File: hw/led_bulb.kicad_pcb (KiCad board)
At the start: 2 copper layers, 136 x 50 mm, 181 parts, among them P1 USB_OTG, P10 CONN_01X04, P11 CONN_01X04, P12 CONN_01X04, P13 CONN_01X04, P14 CONN_01X04, P15 CONN_01X04, P16 CONN_01X04, P17 CONN_01X04, P2 CONN_01X04, P3 CONN_01X04, P4 CONN_01X04, P5 CONN_01X04, P6 CONN_01X04, P7 CONN_01X04, P8 CONN_01X04, P9 CONN_01X04, SW1 SW_RST, SW2 SW_FLASH, U1 CP2102, U3 ESP-12E, U4 AP1117D33

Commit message: Added first version of v4 hardware.
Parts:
- removed HOLE0 (x88): 0.3mm, footprints:0.3mm
- added P18: CONN_01X02, footprints:CONN_2.54mm_1x2_no-outline, F.Cu at (156.4, 125.6)
- added P19: CONN_01X02, footprints:CONN_2.54mm_1x2_no-outline, F.Cu at (149.2, 125.5)
- added P20: CONN_01X02, footprints:CONN_2.54mm_1x2_no-outline, F.Cu at (172.8, 149.2)
- added P21: CONN_01X02, footprints:CONN_2.54mm_1x2_no-outline, F.Cu at (172.8, 142.0)
- added P22: CONN_01X02, footprints:CONN_2.54mm_1x2_no-outline, F.Cu at (149.2, 165.6)
- added P23: CONN_01X02, footprints:CONN_2.54mm_1x2_no-outline, F.Cu at (156.4, 165.6)
- added P24: CONN_01X02, footprints:CONN_2.54mm_1x2_no-outline, F.Cu at (132.9, 142.1)
- added P25: CONN_01X02, footprints:CONN_2.54mm_1x2_no-outline, F.Cu at (132.9, 149.2)
- added P26: CONN_01X02, footprints:CONN_2.54mm_1x2_no-outline, F.Cu at (109.0, 85.1)
- added P27: CONN_01X02, footprints:CONN_2.54mm_1x2_no-outline, F.Cu at (109.0, 78.0)
- added P28: CONN_01X02, footprints:CONN_2.54mm_1x2_no-outline, F.Cu at (109.0, 96.8)
- added P29: CONN_01X02, footprints:CONN_2.54mm_1x2_no-outline, F.Cu at (109.0, 89.7)
- added P30: CONN_01X02, footprints:CONN_2.54mm_1x2_no-outline, F.Cu at (109.0, 108.3)
- added P31: CONN_01X02, footprints:CONN_2.54mm_1x2_no-outline, F.Cu at (109.0, 101.1)
- added P32: CONN_01X02, footprints:CONN_2.54mm_1x2_no-outline, F.Cu at (109.0, 119.7)
- added P33: CONN_01X02, footprints:CONN_2.54mm_1x2_no-outline, F.Cu at (109.0, 112.5)
- P10, P11, P12, P13, P14, P15, P16, P17, P2, P3, P4, P5, P6, P7, P8, P9: value CONN_01X04 -> CONN_01X02; footprint footprints:CONN_2.54mm_1x4_no-outline -> footprints:CONN_2.54mm_1x2_no-outline
- SW1, SW2: footprint footprints:switch_spst_smd_5.5mm_4.5mm -> footprints:switch_spst_smd_5mm_3.5mm
- moved P5 150.2 mm to (102.1, 165.3), turned to 90 degrees
- moved R9 124.8 mm to (112.5, 152.7)
- moved P2 124.1 mm to (102.1, 125.5), turned to 270 degrees
- moved LED9 122.9 mm to (105.7, 126.2)
- moved LED3 122.8 mm to (105.7, 152.2)
- moved LED5 122.8 mm to (105.7, 132.6)
- moved LED11 122.7 mm to (105.8, 165.1)
- moved LED7 122.7 mm to (105.8, 158.6)
- moved LED1 122.6 mm to (105.7, 139.1)
- moved P1 122.6 mm to (103.8, 149.0)
- moved LED12 122.6 mm to (86.2, 145.6)
- moved LED6 122.6 mm to (118.7, 145.6)
- moved C5 122.6 mm to (109.8, 158.0)
- moved C6 122.6 mm to (109.8, 156.3)
- moved LED2 122.6 mm to (112.1, 145.6)
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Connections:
- net DTR renamed Net-(U1-Pad28)
- net RTS renamed Net-(U1-Pad24)
- LED1 pad 1: GPIO16 -> GPIO0
- LED13 pad 3: GND -> Net-(LED13-Pad3)
- LED13 pad 4: V_USB -> Net-(LED13-Pad4)
- LED14 pad 3: GND -> Net-(LED14-Pad3)
- LED14 pad 4: V_USB -> Net-(LED14-Pad4)
- LED15 pad 3: GND -> Net-(LED15-Pad3)
- LED15 pad 4: V_USB -> Net-(LED15-Pad4)
- LED16 pad 3: GND -> Net-(LED16-Pad3)
- LED16 pad 4: V_USB -> Net-(LED16-Pad4)
- LED17 pad 3: GND -> Net-(LED13-Pad3)
- LED17 pad 4: V_USB -> Net-(LED13-Pad4)
- LED18 pad 3: GND -> Net-(LED14-Pad3)
- LED18 pad 4: V_USB -> Net-(LED14-Pad4)
- LED19 pad 3: GND -> Net-(LED15-Pad3)
- LED19 pad 4: V_USB -> Net-(LED15-Pad4)
- LED20 pad 3: GND -> Net-(LED16-Pad3)
- LED20 pad 4: V_USB -> Net-(LED16-Pad4)
- LED21 pad 3: GND -> Net-(LED13-Pad3)
- LED21 pad 4: V_USB -> Net-(LED13-Pad4)
- LED22 pad 3: GND -> Net-(LED14-Pad3)
- LED22 pad 4: V_USB -> Net-(LED14-Pad4)
- LED23 pad 3: GND -> Net-(LED15-Pad3)
- LED23 pad 4: V_USB -> Net-(LED15-Pad4)
- LED24 pad 3: GND -> Net-(LED16-Pad3)
- LED24 pad 4: V_USB -> Net-(LED16-Pad4)
- LED25 pad 3: GND -> Net-(LED13-Pad3)
- LED25 pad 4: V_USB -> Net-(LED13-Pad4)
- LED26 pad 3: GND -> Net-(LED14-Pad3)
- LED26 pad 4: V_USB -> Net-(LED14-Pad4)
- LED27 pad 3: GND -> Net-(LED15-Pad3)
- LED27 pad 4: V_USB -> Net-(LED15-Pad4)
- LED28 pad 3: GND -> Net-(LED16-Pad3)
- LED28 pad 4: V_USB -> Net-(LED16-Pad4)
- LED29 pad 3: GND -> Net-(LED13-Pad3)
- LED29 pad 4: V_USB -> Net-(LED13-Pad4)
- LED30 pad 3: GND -> Net-(LED14-Pad3)
- LED30 pad 4: V_USB -> Net-(LED14-Pad4)
- LED31 pad 3: GND -> Net-(LED15-Pad3)
- LED31 pad 4: V_USB -> Net-(LED15-Pad4)
- LED32 pad 3: GND -> Net-(LED16-Pad3)
- LED32 pad 4: V_USB -> Net-(LED16-Pad4)
- LED33 pad 3: GND -> Net-(LED13-Pad3)
- LED33 pad 4: V_USB -> Net-(LED13-Pad4)
- LED34 pad 3: GND -> Net-(LED14-Pad3)
- LED34 pad 4: V_USB -> Net-(LED14-Pad4)
- LED35 pad 3: GND -> Net-(LED15-Pad3)
- LED35 pad 4: V_USB -> Net-(LED15-Pad4)
- LED36 pad 3: GND -> Net-(LED16-Pad3)
- LED36 pad 4: V_USB -> Net-(LED16-Pad4)
- LED37 pad 3: GND -> Net-(LED13-Pad3)
- LED37 pad 4: V_USB -> Net-(LED13-Pad4)
- LED38 pad 3: GND -> Net-(LED14-Pad3)
- LED38 pad 4: V_USB -> Net-(LED14-Pad4)
- LED39 pad 3: GND -> Net-(LED15-Pad3)
- LED39 pad 4: V_USB -> Net-(LED15-Pad4)
- LED40 pad 3: GND -> Net-(LED16-Pad3)
- LED40 pad 4: V_USB -> Net-(LED16-Pad4)
- LED41 pad 3: GND -> Net-(LED41-Pad3)
- LED41 pad 4: V_USB -> Net-(LED41-Pad4)
- LED42 pad 3: GND -> Net-(LED42-Pad3)
- LED42 pad 4: V_USB -> Net-(LED42-Pad4)
- LED43 pad 3: GND -> Net-(LED43-Pad3)
- LED43 pad 4: V_USB -> Net-(LED43-Pad4)
- LED44 pad 3: GND -> Net-(LED44-Pad3)
- LED44 pad 4: V_USB -> Net-(LED44-Pad4)
- LED45 pad 3: GND -> Net-(LED42-Pad3)
- LED45 pad 4: V_USB -> Net-(LED42-Pad4)
- LED46 pad 3: GND -> Net-(LED41-Pad3)
- LED46 pad 4: V_USB -> Net-(LED41-Pad4)
- LED47 pad 3: GND -> Net-(LED43-Pad3)
- LED47 pad 4: V_USB -> Net-(LED43-Pad4)
- LED48 pad 3: GND -> Net-(LED44-Pad3)
- LED48 pad 4: V_USB -> Net-(LED44-Pad4)
- LED49 pad 3: GND -> Net-(LED42-Pad3)
- LED49 pad 4: V_USB -> Net-(LED42-Pad4)
- LED50 pad 3: GND -> Net-(LED41-Pad3)
- LED50 pad 4: V_USB -> Net-(LED41-Pad4)
- LED51 pad 3: GND -> Net-(LED43-Pad3)
- LED51 pad 4: V_USB -> Net-(LED43-Pad4)
- LED52 pad 3: GND -> Net-(LED44-Pad3)
- LED52 pad 4: V_USB -> Net-(LED44-Pad4)
- LED53 pad 3: GND -> Net-(LED41-Pad3)
- LED53 pad 4: V_USB -> Net-(LED41-Pad4)
- P10 pad 1: Net-(LED37-Pad6) -> Net-(LED13-Pad2)
- P10 pad 2: Net-(LED37-Pad5) -> Net-(LED13-Pad1)
- P11 pad 1: Net-(LED38-Pad6) -> Net-(LED13-Pad3)
- P11 pad 2: Net-(LED38-Pad5) -> Net-(LED13-Pad4)
- P12 pad 1: Net-(LED39-Pad6) -> Net-(LED14-Pad2)
- P12 pad 2: Net-(LED39-Pad5) -> Net-(LED14-Pad1)
- P13 pad 1: Net-(LED40-Pad6) -> Net-(LED14-Pad3)
- P13 pad 2: Net-(LED40-Pad5) -> Net-(LED14-Pad4)
- P14 pad 1: GND -> Net-(LED15-Pad2)
- P14 pad 2: V_USB -> Net-(LED15-Pad1)
- P15 pad 1: GND -> Net-(LED15-Pad3)
- P15 pad 2: V_USB -> Net-(LED15-Pad4)
- P16 pad 1: GND -> Net-(LED16-Pad2)
- P16 pad 2: V_USB -> Net-(LED16-Pad1)
- P17 pad 1: GND -> Net-(LED16-Pad3)
- P17 pad 2: V_USB -> Net-(LED16-Pad4)
- P3 pad 1: Net-(LED10-Pad6) -> V_USB
- P3 pad 2: Net-(LED10-Pad5) -> GND
- P4 pad 1: Net-(LED11-Pad6) -> Net-(LED10-Pad6)
- P4 pad 2: Net-(LED11-Pad5) -> Net-(LED10-Pad5)
- P5 pad 1: Net-(LED12-Pad6) -> V_USB
- P5 pad 2: Net-(LED12-Pad5) -> GND
- P6 pad 1: GND -> Net-(LED11-Pad6)
- P6 pad 2: V_USB -> Net-(LED11-Pad5)
- P7 pad 1: GND -> V_USB
- P7 pad 2: V_USB -> GND
- P8 pad 1: GND -> Net-(LED12-Pad6)
- P8 pad 2: V_USB -> Net-(LED12-Pad5)
- P9 pad 1: GND -> V_USB
- P9 pad 2: V_USB -> GND
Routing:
- net GND: track 595.8 -> 0.00 mm, vias 30 -> 0
- net V_USB: track 508.1 -> 0.00 mm, vias 42 -> 0
- net V_3.3: track 76.2 -> 0.00 mm, vias 3 -> 0
- net GPIO16: track 28.6 -> 0.00 mm, vias 1 -> 0
- net TX: track 27.7 -> 0.00 mm, vias 3 -> 0
- net Net-(R8-Pad1): track 21.2 -> 0.00 mm, vias 1 -> 0
- net GPIO0: track 18.6 -> 0.00 mm
- net GPIO2: track 16.8 -> 0.00 mm, vias 1 -> 0
- net nRST: track 12.5 -> 0.00 mm
- net GPIO15: track 12.2 -> 0.00 mm, vias 1 -> 0
- net USB_D+: track 11.5 -> 0.00 mm, vias 2 -> 0
- net USB_D-: track 9.94 -> 0.00 mm, vias 1 -> 0
- net EN: track 9.22 -> 0.00 mm
- net LED4_DATA: track 8.03 -> 0.00 mm, vias 1 -> 0
- net LED2_CLK: track 7.80 -> 0.00 mm, vias 1 -> 0
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- removed copper zone on B.Cu, net GND
- removed copper zone on B.Cu, net V_USB
- removed copper zone on F.Cu, net V_USB
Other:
- board size 136 x 50 mm -> 92.4 x 91.4 mm
- board text added: "esp8266_apa102_bulb v4"
- board text removed: "CLK_IN"
- board text removed: "CLK_OUT"
- board text removed: "D_IN"
- board text removed: "D_OUT"
- board text removed: "GND"
- board text removed: "VCC"
- board text removed: "esp8266_apa102_bulb v3.0"

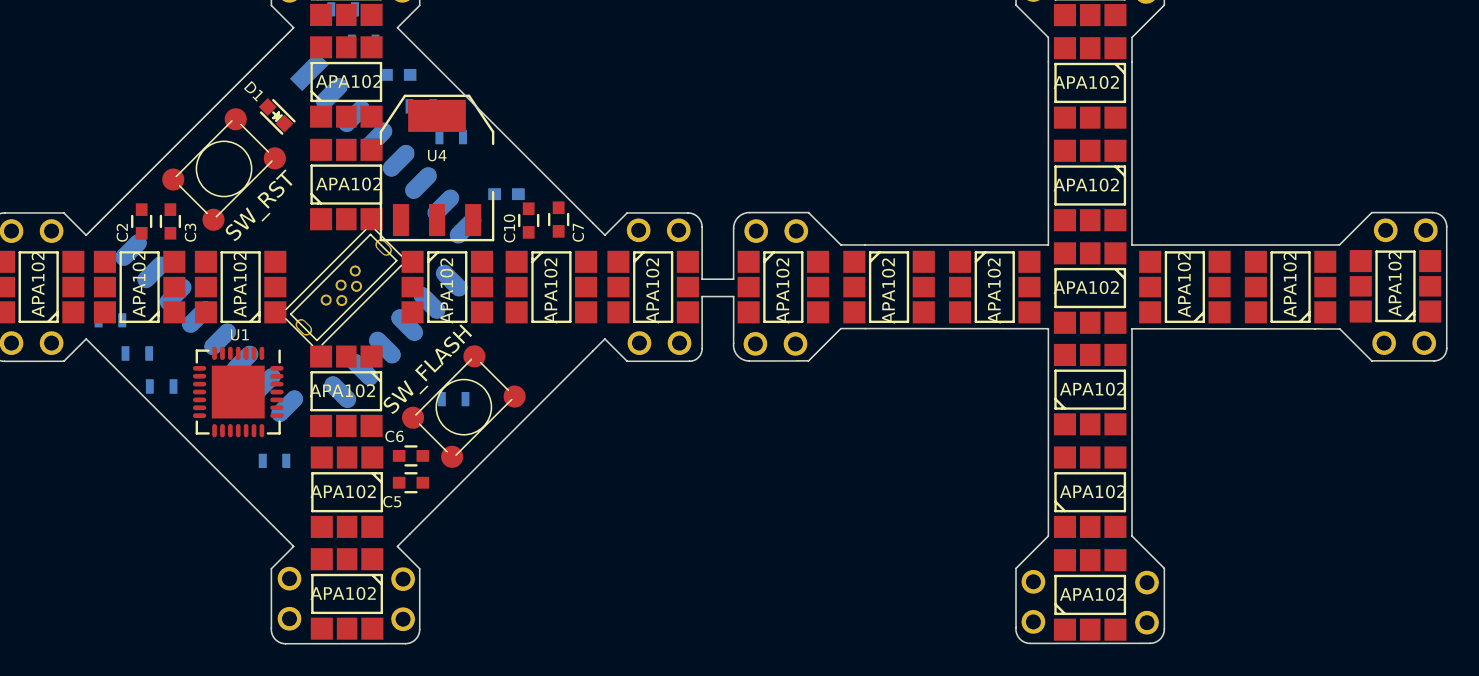
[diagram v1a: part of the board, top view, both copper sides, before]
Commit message: Revised connectors and labels.
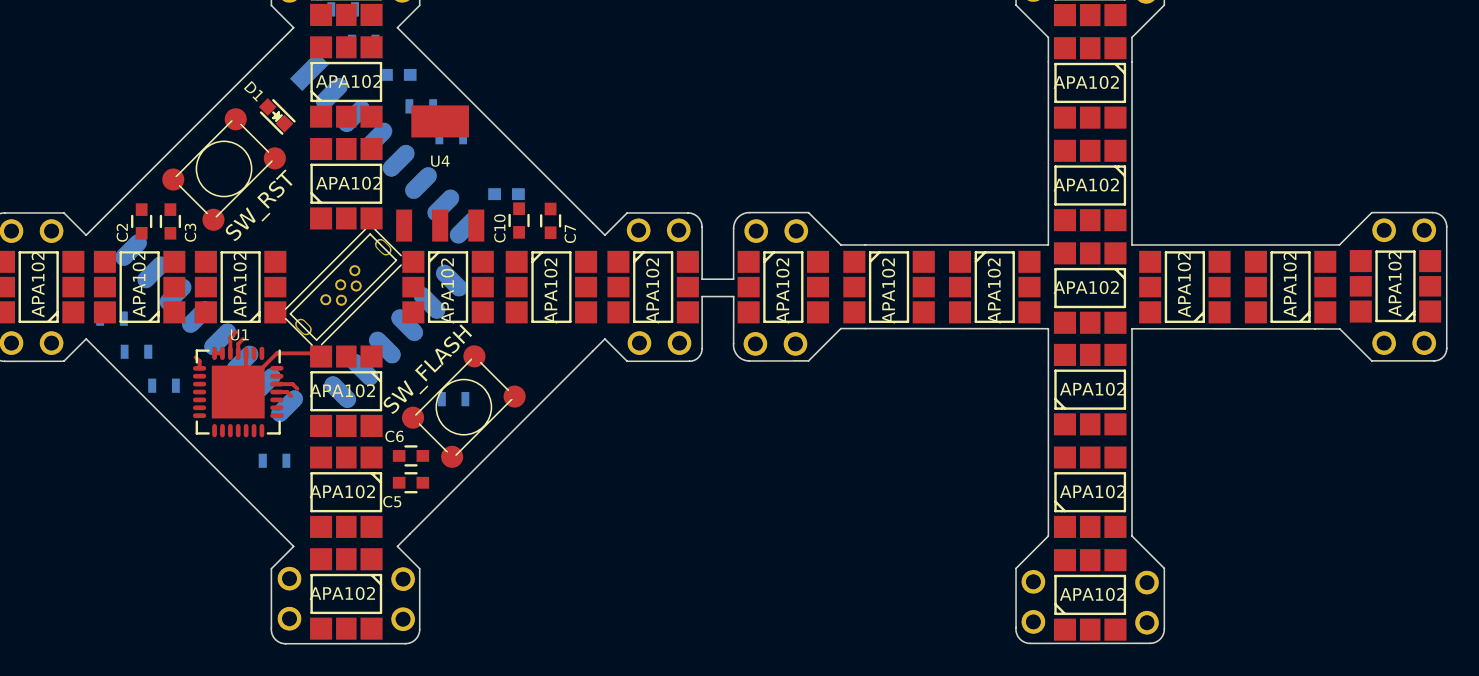
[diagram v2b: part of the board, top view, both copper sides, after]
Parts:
- U4: footprint TO_SOT_Packages_SMD:SOT-223 -> footprints:ams-1117-3.3_no-outline
- moved C10 0.61 mm to (116.7, 141.4)
- moved C7 0.52 mm to (118.7, 141.4)
- moved U4 0.40 mm to (111.7, 138.4)
- moved R2 0.16 mm to (94.2, 151.8)
- moved R8 0.15 mm to (90.8, 147.6)
- moved R1 0.12 mm to (92.4, 149.7)
- moved P21 0.10 mm to (172.8, 142.0), turned to 0 degrees
- moved LED2 0.05 mm to (112.2, 145.6)
- turned P10 to 0 degrees
- turned P11 to 0 degrees
- turned P12 to 0 degrees
- turned P13 to 0 degrees
- turned P14 to 0 degrees
- turned P15 to 0 degrees
- turned P16 to 0 degrees
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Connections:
- U1 pad 29: (no net) -> GND
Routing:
- net GND: track 0.00 -> 15.3 mm
- net USB_D-: track 0.00 -> 1.49 mm
- net Net-(R8-Pad1): track 0.00 -> 1.42 mm
- net USB_D+: track 0.00 -> 1.02 mm
- net TX: track 0.00 -> 1.00 mm
- net V_USB: track 0.00 -> 0.80 mm
- net V_3.3: track 0.00 -> 0.50 mm
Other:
- board text added: "->"
- board text added: "CLK"
- board text added: "D"
- board text added: "GND"
- board text added: "VCC"
- board text added: "esp8266_apa102_bulb v4.0"
- board text removed: "esp8266_apa102_bulb v4"

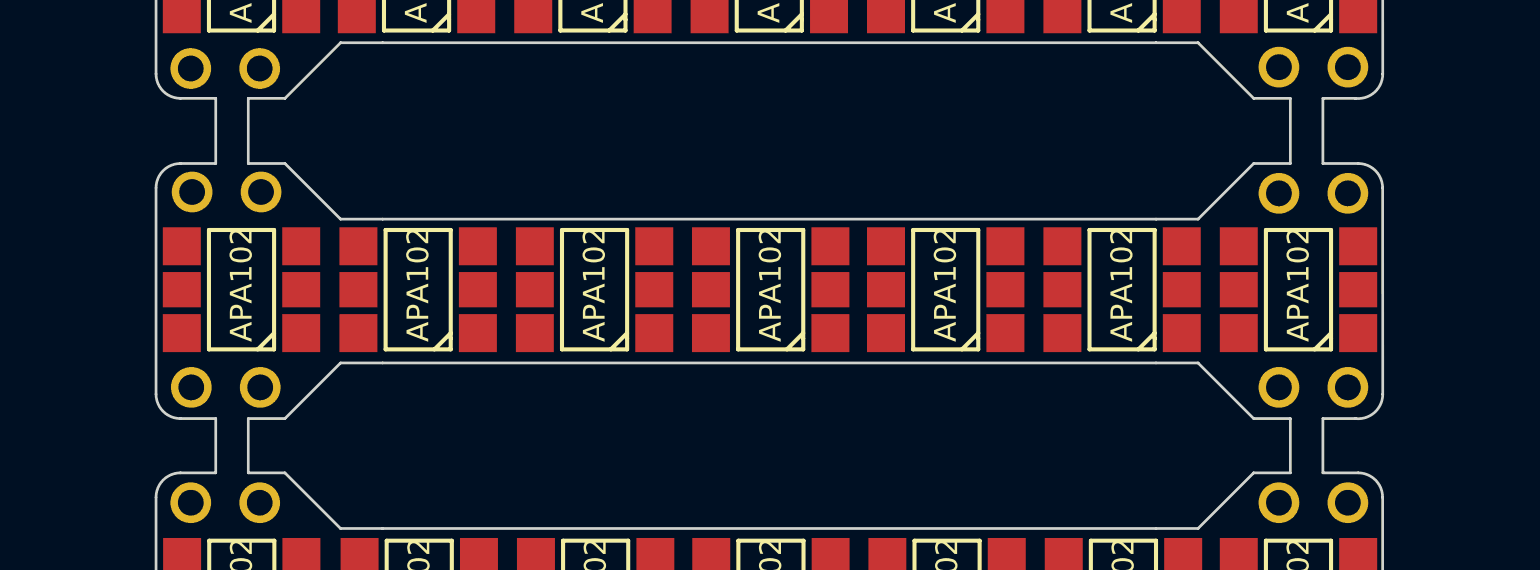
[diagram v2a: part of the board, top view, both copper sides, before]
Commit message: Added missing label.
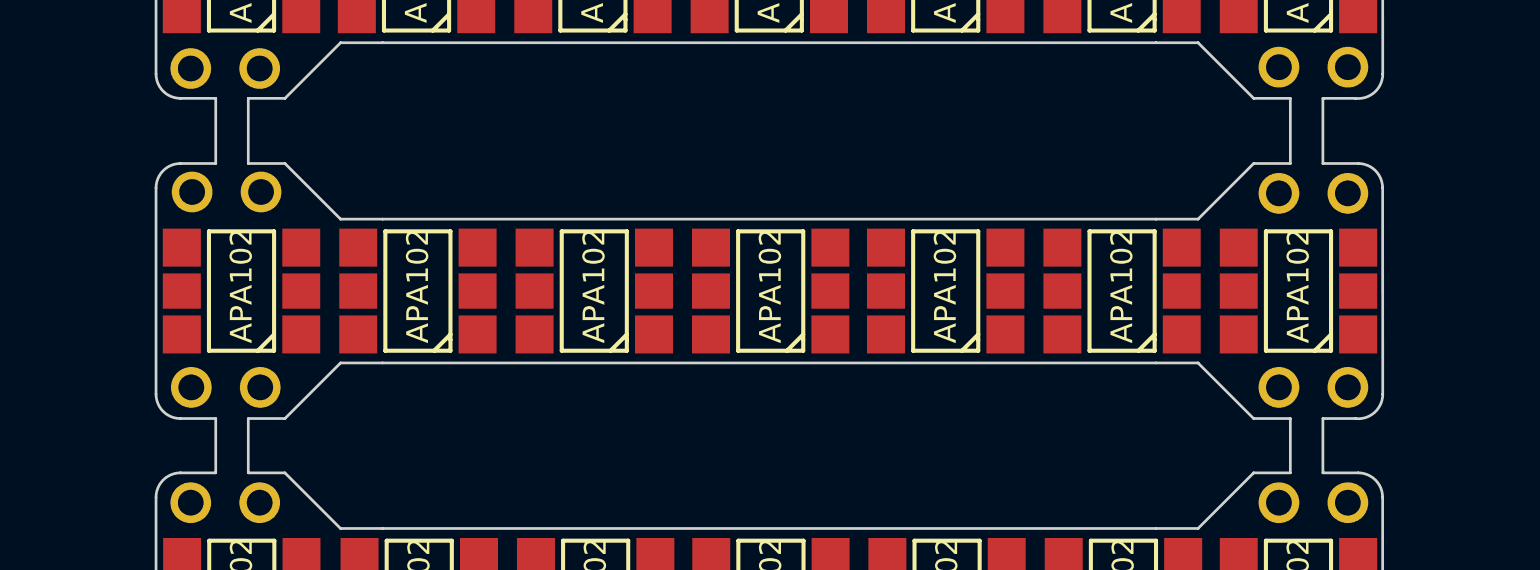
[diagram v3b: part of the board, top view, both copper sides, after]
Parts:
- moved LED30 0.05 mm to (122.6, 93.3)
- moved LED34 0.05 mm to (116.1, 93.3)
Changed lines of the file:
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@@
     (links 302)
     (no_connects 296)
-    (area 78.0316 71.860714 180.568401 173.3184)
+    (area 82.996992 76.749999 175.498858 168.255113)
     (thickness 1.6)
     (drawings 266)
@@
   )
   (module APA102:APA102 (layer F.Cu)
-    (at 109.6 93.25 90)
+    (at 109.6 93.3 90)
     (fp_text reference LED38 (at 5.8 0 90) (layer F.SilkS) hide
       (effects (font (size 1.5 1.5) (thickness 0.15)))
@@
   )
   (module APA102:APA102 (layer F.Cu)
-    (at 135.55 93.25 90)
+    (at 135.55 93.3 90)
     (fp_text reference LED22 (at 5.9 0 90) (layer F.SilkS) hide
       (effects (font (size 1.5 1.5) (thickness 0.15)))
@@
   )
   (module APA102:APA102 (layer F.Cu)
-    (at 129.1 93.25 90)
+    (at 129.1 93.3 90)
     (fp_text reference LED26 (at 5.9 0 90) (layer F.SilkS) hide
       (effects (font (size 1.5 1.5) (thickness 0.15)))
@@
   )
   (module APA102:APA102 (layer F.Cu)
-    (at 142.05 93.25 90)
+    (at 142.05 93.3 90)
     (fp_text reference LED18 (at 5.9 -0.1 90) (layer F.SilkS) hide
       (effects (font (size 1.5 1.5) (thickness 0.15)))
@@
   )
   (module APA102:APA102 (layer F.Cu)
-    (at 148.55 93.25 90)
+    (at 148.55 93.3 90)
     (fp_text reference LED14 (at 5.8 -0.2 90) (layer F.SilkS) hide
       (effects (font (size 1.5 1.5) (thickness 0.15)))
@@
   )
   (module APA102:APA102 (layer F.Cu)
-    (at 122.61 93.25 90)
+    (at 122.6 93.3 90)
     (fp_text reference LED30 (at 5.8 0 90) (layer F.SilkS) hide
       (effects (font (size 1.5 1.5) (thickness 0.15)))
@@
   )
   (module APA102:APA102 (layer F.Cu)
-    (at 116.11 93.25 90)
+    (at 116.1 93.3 90)
     (fp_text reference LED34 (at 5.9 0 90) (layer F.SilkS) hide
       (effects (font (size 1.5 1.5) (thickness 0.15)))

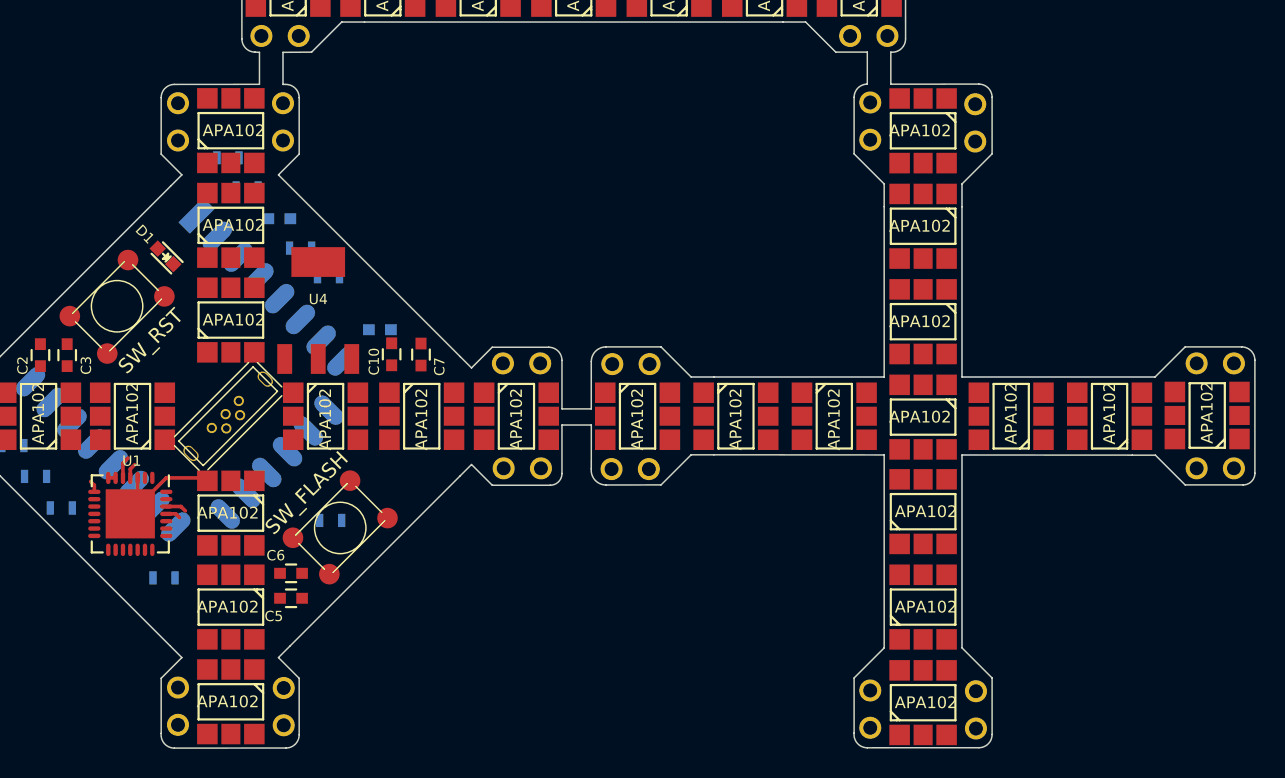
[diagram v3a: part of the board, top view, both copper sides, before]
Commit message: Rotated bottom footprints to be more intuitive.
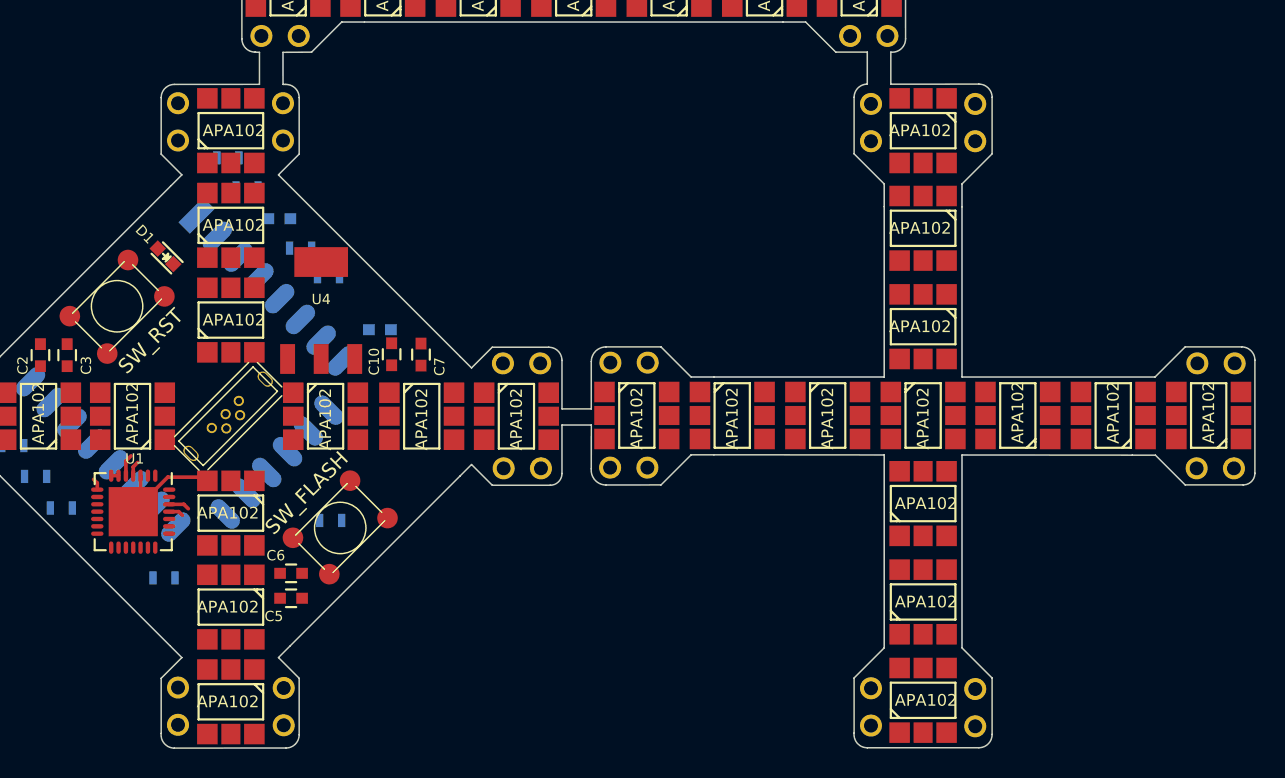
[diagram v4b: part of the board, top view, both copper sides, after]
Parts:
- moved P19 28.8 mm to (132.8, 149.1), turned to 180 degrees
- moved P23 28.7 mm to (172.8, 142.0), turned to 0 degrees
- moved P18 28.7 mm to (132.8, 141.9), turned to 180 degrees
- moved P20 28.7 mm to (156.4, 125.6), turned to 90 degrees
- moved P22 28.7 mm to (172.8, 149.2), turned to 0 degrees
- moved P21 28.6 mm to (149.3, 125.6), turned to 90 degrees
- moved P25 28.6 mm to (156.4, 165.4), turned to 270 degrees
- moved P24 28.5 mm to (149.3, 165.4), turned to 270 degrees
- moved LED43 27.6 mm to (172.3, 145.6), turned to 90 degrees
- moved LED41 27.5 mm to (133.3, 145.6), turned to 270 degrees
- moved LED44 27.4 mm to (152.8, 164.9), turned to 0 degrees
- moved LED42 27.4 mm to (152.8, 126.2), turned to 180 degrees
- moved LED47 18.4 mm to (165.8, 145.6), turned to 90 degrees
- moved LED46 18.3 mm to (139.8, 145.6), turned to 270 degrees
- moved LED45 18.0 mm to (152.8, 132.8), turned to 180 degrees
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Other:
- net class Power: trace_width 0.4 -> 0.25
